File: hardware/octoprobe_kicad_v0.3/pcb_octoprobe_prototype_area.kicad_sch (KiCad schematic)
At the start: 15 parts, among them J1101 Conn_01x20, J1102 Conn_01x20, J1103 Conn_01x20

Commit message: PCB: Octobus
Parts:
- J1101, J1102, J1103: footprint 00_project_library:PinSocket_2x20_P2.54mm_Vertical-mirrored-stackable -> 00_project_library:PinSocket_2x20_P2.54mm_Vertical-stackable_squarepad; symbol Connector_Generic:Conn_02x20_Odd_Even -> Connector_Generic:Conn_01x40; now in the parts list
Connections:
- net at J1101.10 (Pin_10), J1102.10 (Pin_10), J1103.10 (Pin_10): no longer J1101.9 (Pin_9), J1102.9 (Pin_9), J1103.9 (Pin_9)
- net at J1101.11 (Pin_11), J1102.11 (Pin_11), J1103.11 (Pin_11): no longer J1101.12 (Pin_12), J1102.12 (Pin_12), J1103.12 (Pin_12)
- net at J1101.13 (Pin_13), J1102.13 (Pin_13), J1103.13 (Pin_13): no longer J1101.14 (Pin_14), J1102.14 (Pin_14), J1103.14 (Pin_14)
- net at J1101.15 (Pin_15), J1102.15 (Pin_15), J1103.15 (Pin_15): no longer J1101.16 (Pin_16), J1102.16 (Pin_16), J1103.16 (Pin_16)
- net at J1101.17 (Pin_17), J1102.17 (Pin_17), J1103.17 (Pin_17): no longer J1101.18 (Pin_18), J1102.18 (Pin_18), J1103.18 (Pin_18)
- net at J1101.19 (Pin_19), J1102.19 (Pin_19), J1103.19 (Pin_19): no longer J1101.20 (Pin_20), J1102.20 (Pin_20), J1103.20 (Pin_20)
- net at J1101.21 (Pin_21), J1102.21 (Pin_21), J1103.21 (Pin_21): no longer J1101.22 (Pin_22), J1102.22 (Pin_22), J1103.22 (Pin_22)
- net at J1101.23 (Pin_23), J1102.23 (Pin_23), J1103.23 (Pin_23): no longer J1101.24 (Pin_24), J1102.24 (Pin_24), J1103.24 (Pin_24)
- net at J1101.25 (Pin_25), J1102.25 (Pin_25), J1103.25 (Pin_25): no longer J1101.26 (Pin_26), J1102.26 (Pin_26), J1103.26 (Pin_26)
- net at J1101.27 (Pin_27), J1102.27 (Pin_27), J1103.27 (Pin_27): no longer J1101.28 (Pin_28), J1102.28 (Pin_28), J1103.28 (Pin_28)
- net at J1101.29 (Pin_29), J1102.29 (Pin_29), J1103.29 (Pin_29): no longer J1101.30 (Pin_30), J1102.30 (Pin_30), J1103.30 (Pin_30)
- net at J1101.31 (Pin_31), J1102.31 (Pin_31), J1103.31 (Pin_31): no longer J1101.32 (Pin_32), J1102.32 (Pin_32), J1103.32 (Pin_32)
- net at J1101.33 (Pin_33), J1102.33 (Pin_33), J1103.33 (Pin_33): no longer J1101.34 (Pin_34), J1102.34 (Pin_34), J1103.34 (Pin_34)
- net at J1101.35 (Pin_35), J1102.35 (Pin_35), J1103.35 (Pin_35): no longer J1101.36 (Pin_36), J1102.36 (Pin_36), J1103.36 (Pin_36)
- net at J1101.5 (Pin_5), J1102.5 (Pin_5), J1103.5 (Pin_5): no longer J1101.6 (Pin_6), J1102.6 (Pin_6), J1103.6 (Pin_6)
- net at J1101.7 (Pin_7), J1102.7 (Pin_7), J1103.7 (Pin_7): no longer J1101.8 (Pin_8), J1102.8 (Pin_8), J1103.8 (Pin_8)
- new net: J1101.12 (Pin_12), J1102.12 (Pin_12), J1103.12 (Pin_12)
- new net: J1101.14 (Pin_14), J1102.14 (Pin_14), J1103.14 (Pin_14)
- new net: J1101.16 (Pin_16), J1102.16 (Pin_16), J1103.16 (Pin_16)
- new net: J1101.18 (Pin_18), J1102.18 (Pin_18), J1103.18 (Pin_18)
- new net: J1101.20 (Pin_20), J1102.20 (Pin_20), J1103.20 (Pin_20)
- new net: J1101.22 (Pin_22), J1102.22 (Pin_22), J1103.22 (Pin_22)
- new net: J1101.24 (Pin_24), J1102.24 (Pin_24), J1103.24 (Pin_24)
- new net: J1101.26 (Pin_26), J1102.26 (Pin_26), J1103.26 (Pin_26)
- new net: J1101.28 (Pin_28), J1102.28 (Pin_28), J1103.28 (Pin_28)
- new net: J1101.30 (Pin_30), J1102.30 (Pin_30), J1103.30 (Pin_30)
- new net: J1101.32 (Pin_32), J1102.32 (Pin_32), J1103.32 (Pin_32)
- new net: J1101.34 (Pin_34), J1102.34 (Pin_34), J1103.34 (Pin_34)
- new net: J1101.36 (Pin_36), J1102.36 (Pin_36), J1103.36 (Pin_36)
- new net: J1101.6 (Pin_6), J1102.6 (Pin_6), J1103.6 (Pin_6)
- new net: J1101.8 (Pin_8), J1102.8 (Pin_8), J1103.8 (Pin_8)
- new net: J1101.9 (Pin_9), J1102.9 (Pin_9), J1103.9 (Pin_9)
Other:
- moved on the sheet: J1101, J1102, J1103

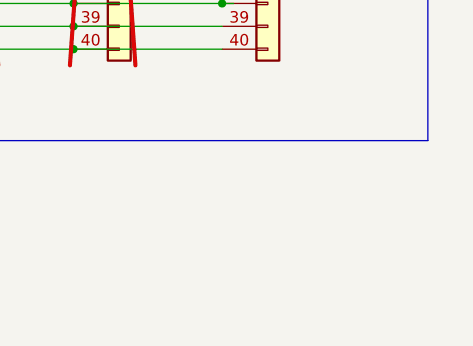
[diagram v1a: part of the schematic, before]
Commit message: PCB: Add "Open Hardware"
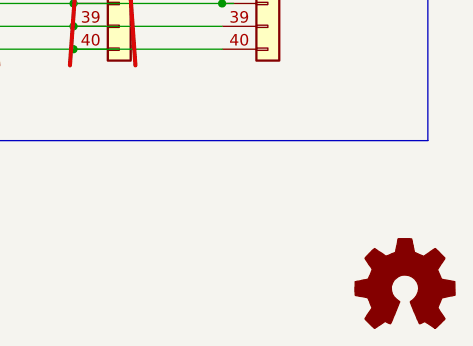
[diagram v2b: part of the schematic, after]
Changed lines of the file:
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@@
+	)
+	(symbol
+		(lib_id "Graphic:Logo_Open_Hardware_Small")
+		(at 275.59 173.99 0)
+		(unit 1)
+		(exclude_from_sim yes)
+		(in_bom no)
+		(on_board no)
+		(dnp no)
+		(fields_autoplaced yes)
+		(property "Reference" "#SYM1301"
+			(at 275.59 167.005 0)
+			(effects
+				(font
+					(size 1.27 1.27)
+				)
+				(hide yes)
+			)
+		)
+		(property "Value" "Logo_Open_Hardware_Small"
+			(at 275.59 179.705 0)
+			(effects
+				(font
+					(size 1.27 1.27)
+				)
+				(hide yes)
+			)
+		)
+		(property "Footprint" ""
+			(at 275.59 173.99 0)
+			(effects
+				(font
+					(size 1.27 1.27)
+				)
+				(hide yes)
+			)
+		)
+		(property "Datasheet" "~"
+			(at 275.59 173.99 0)
+			(effects
+				(font
+					(size 1.27 1.27)
+				)
+				(hide yes)
+			)
+		)
+		(property "Description" "Open Hardware logo, small"
+			(at 275.59 173.99 0)
+			(effects
+				(font
+					(size 1.27 1.27)
+				)
+				(hide yes)
+			)
+		)
+		(instances
+			(project "pcb_octoprobe"
+				(path "/35c47459-45a7-4753-acae-c8b47e7575e1/290edc0f-259a-4a81-bb28-767ae8aa5342"
+					(reference "#SYM1301")
+					(unit 1)
+				)
+			)
+		)
 	)
 	(symbol

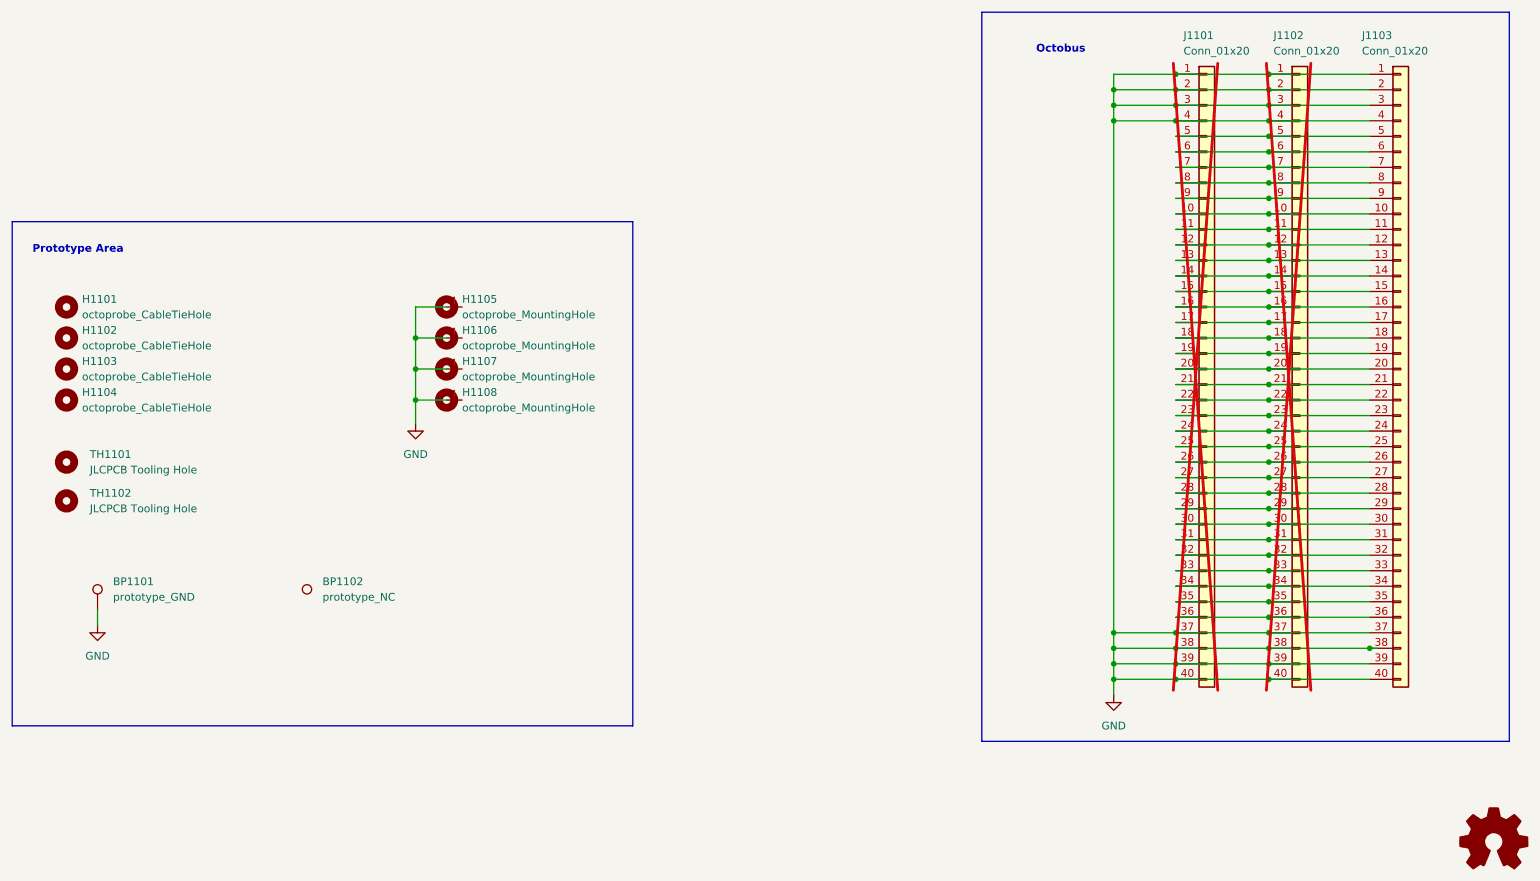
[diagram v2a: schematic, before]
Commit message: PCB: Production files ready
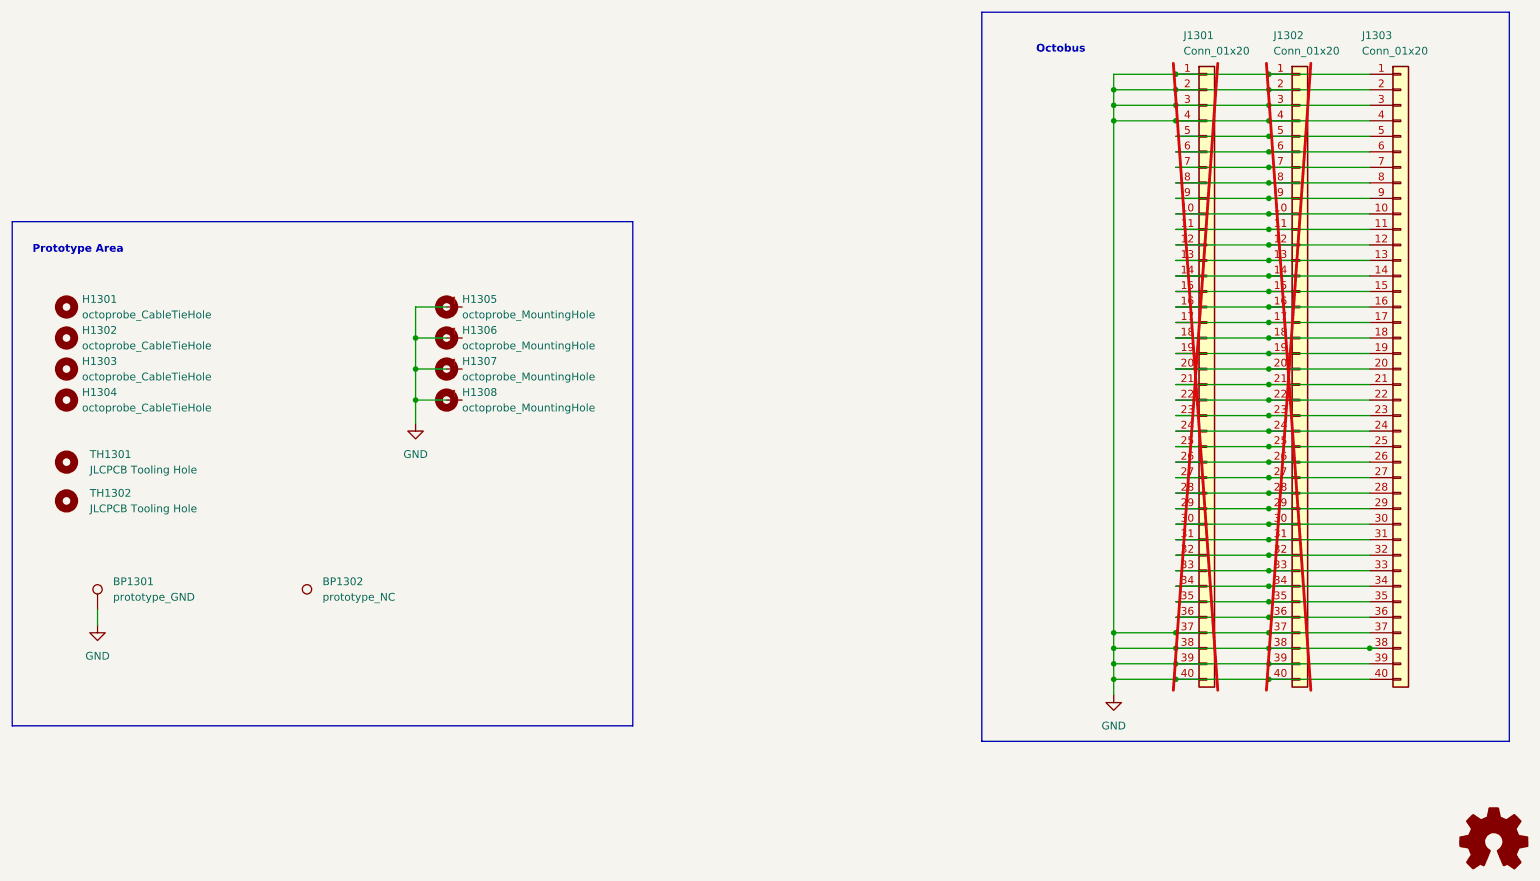
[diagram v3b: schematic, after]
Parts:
- J1301: renamed from J1101; now left out of the parts list
- J1302: renamed from J1102; now left out of the parts list
- J1303: renamed from J1103; now left out of the parts list
- renumbered BP1101 to BP1301, BP1102 to BP1302, H1101 to H1301, H1102 to H1302, H1103 to H1303, H1104 to H1304, H1105 to H1305, H1106 to H1306, H1107 to H1307, H1108 to H1308, TH1101 to TH1301, TH1102 to TH1302
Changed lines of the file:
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@@
 	(title_block
 		(title "Octoprobe tentacle")
-		(date "2024-07-31")
+		(date "2024-08-04")
 		(rev "0.3")
 		(company "Hans Märki, Märki Informatik")
@@
 		(dnp no)
 		(fields_autoplaced yes)
-		(property "Reference" "H1108"
+		(property "Reference" "H1308"
 			(at 106.68 100.3299 0)
 			(effects
@@
 			(project "pcb_octoprobe"
 				(path "/35c47459-45a7-4753-acae-c8b47e7575e1/290edc0f-259a-4a81-bb28-767ae8aa5342"
-					(reference "H1108")
+					(reference "H1308")
 					(unit 1)
 				)
@@
 		(dnp no)
 		(fields_autoplaced yes)
-		(property "Reference" "H1105"
+		(property "Reference" "H1305"
 			(at 106.68 85.0899 0)
 			(effects
@@
 			(project "pcb_octoprobe"
 				(path "/35c47459-45a7-4753-acae-c8b47e7575e1/290edc0f-259a-4a81-bb28-767ae8aa5342"
-					(reference "H1105")
+					(reference "H1305")
 					(unit 1)
 				)
@@
 		(unit 1)
 		(exclude_from_sim no)
-		(in_bom yes)
+		(in_bom no)
 		(on_board yes)
 		(dnp yes)
-		(property "Reference" "J1101"
+		(property "Reference" "J1301"
 			(at 224.79 41.91 0)
 			(effects
@@
 			(project "pcb_octoprobe"
 				(path "/35c47459-45a7-4753-acae-c8b47e7575e1/290edc0f-259a-4a81-bb28-767ae8aa5342"
-					(reference "J1101")
+					(reference "J1301")
 					(unit 1)
 				)
@@
 		(dnp no)
 		(fields_autoplaced yes)
-		(property "Reference" "H1106"
+		(property "Reference" "H1306"
 			(at 106.68 90.1699 0)
 			(effects
@@
 			(project "pcb_octoprobe"
 				(path "/35c47459-45a7-4753-acae-c8b47e7575e1/290edc0f-259a-4a81-bb28-767ae8aa5342"
-					(reference "H1106")
+					(reference "H1306")
 					(unit 1)
 				)
@@
 		(dnp no)
 		(fields_autoplaced yes)
-		(property "Reference" "#PWR01102"
+		(property "Reference" "#PWR01302"
 			(at 99.06 111.76 0)
 			(effects
@@
 			(project "pcb_octoprobe"
 				(path "/35c47459-45a7-4753-acae-c8b47e7575e1/290edc0f-259a-4a81-bb28-767ae8aa5342"
-					(reference "#PWR01102")
+					(reference "#PWR01302")
 					(unit 1)
 				)
@@
 		(dnp no)
 		(fields_autoplaced yes)
-		(property "Reference" "H1103"
+		(property "Reference" "H1303"
 			(at 44.45 95.2499 0)
 			(effects
@@
 			(project "pcb_octoprobe"
 				(path "/35c47459-45a7-4753-acae-c8b47e7575e1/290edc0f-259a-4a81-bb28-767ae8aa5342"
-					(reference "H1103")
+					(reference "H1303")
 					(unit 1)
 				)
@@
 		(dnp no)
 		(fields_autoplaced yes)
-		(property "Reference" "H1107"
+		(property "Reference" "H1307"
 			(at 106.68 95.2499 0)
 			(effects
@@
 			(project "pcb_octoprobe"
 				(path "/35c47459-45a7-4753-acae-c8b47e7575e1/290edc0f-259a-4a81-bb28-767ae8aa5342"
-					(reference "H1107")
+					(reference "H1307")
 					(unit 1)
 				)
@@
 		(dnp no)
 		(fields_autoplaced yes)
-		(property "Reference" "#PWR01101"
+		(property "Reference" "#PWR01301"
 			(at 46.99 144.78 0)
 			(effects
@@
 			(project "pcb_octoprobe"
 				(path "/35c47459-45a7-4753-acae-c8b47e7575e1/290edc0f-259a-4a81-bb28-767ae8aa5342"
-					(reference "#PWR01101")
+					(reference "#PWR01301")
 					(unit 1)
 				)
@@
 		(on_board yes)
 		(dnp no)
-		(property "Reference" "TH1102"
+		(property "Reference" "TH1302"
 			(at 45.72 116.84 0)
 			(effects
@@
 			(project "pcb_octoprobe"
 				(path "/35c47459-45a7-4753-acae-c8b47e7575e1/290edc0f-259a-4a81-bb28-767ae8aa5342"
-					(reference "TH1102")
+					(reference "TH1302")
 					(unit 1)
 				)
@@
 		(on_board yes)
 		(dnp no)
-		(property "Reference" "TH1101"
+		(property "Reference" "TH1301"
 			(at 45.72 110.49 0)
 			(effects
@@
 			(project ""
 				(path "/35c47459-45a7-4753-acae-c8b47e7575e1/290edc0f-259a-4a81-bb28-767ae8aa5342"
-					(reference "TH1101")
+					(reference "TH1301")
 					(unit 1)
 				)
@@
 		(dnp no)
 		(fields_autoplaced yes)
-		(property "Reference" "H1101"
+		(property "Reference" "H1301"
 			(at 44.45 85.0899 0)
 			(effects
@@
 			(project "pcb_octoprobe"
 				(path "/35c47459-45a7-4753-acae-c8b47e7575e1/290edc0f-259a-4a81-bb28-767ae8aa5342"
-					(reference "H1101")
+					(reference "H1301")
 					(unit 1)
 				)
@@
 		(dnp no)
 		(fields_autoplaced yes)
-		(property "Reference" "#PWR01103"
+		(property "Reference" "#PWR01303"
 			(at 213.36 156.21 0)
 			(effects
@@
 			(project "pcb_octoprobe"
 				(path "/35c47459-45a7-4753-acae-c8b47e7575e1/290edc0f-259a-4a81-bb28-767ae8aa5342"
-					(reference "#PWR01103")
+					(reference "#PWR01303")
 					(unit 1)
 				)
@@
 		(dnp no)
 		(fields_autoplaced yes)
-		(property "Reference" "H1102"
+		(property "Reference" "H1302"
 			(at 44.45 90.1699 0)
 			(effects
@@
 			(project "pcb_octoprobe"
 				(path "/35c47459-45a7-4753-acae-c8b47e7575e1/290edc0f-259a-4a81-bb28-767ae8aa5342"
-					(reference "H1102")
+					(reference "H1302")
 					(unit 1)
 				)
@@
 		(dnp no)
 		(fields_autoplaced yes)
-		(property "Reference" "BP1101"
+		(property "Reference" "BP1301"
 			(at 49.53 131.3179 0)
 			(effects
@@
 			(project "pcb_octoprobe"
 				(path "/35c47459-45a7-4753-acae-c8b47e7575e1/290edc0f-259a-4a81-bb28-767ae8aa5342"
-					(reference "BP1101")
+					(reference "BP1301")
 					(unit 1)
 				)
@@
 		(unit 1)
 		(exclude_from_sim no)
-		(in_bom yes)
+		(in_bom no)
 		(on_board yes)
 		(dnp no)
-		(property "Reference" "J1103"
+		(property "Reference" "J1303"
 			(at 254 41.91 0)
 			(effects
@@
 			(project "pcb_octoprobe"
 				(path "/35c47459-45a7-4753-acae-c8b47e7575e1/290edc0f-259a-4a81-bb28-767ae8aa5342"
-					(reference "J1103")
+					(reference "J1303")
 					(unit 1)
 				)
@@
 		(dnp no)
 		(fields_autoplaced yes)
-		(property "Reference" "H1104"
+		(property "Reference" "H1304"
 			(at 44.45 100.3299 0)
 			(effects
@@
 			(project "pcb_octoprobe"
 				(path "/35c47459-45a7-4753-acae-c8b47e7575e1/290edc0f-259a-4a81-bb28-767ae8aa5342"
-					(reference "H1104")
+					(reference "H1304")
 					(unit 1)
 				)
@@
 		(unit 1)
 		(exclude_from_sim no)
-		(in_bom yes)
+		(in_bom no)
 		(on_board yes)
 		(dnp yes)
-		(property "Reference" "J1102"
+		(property "Reference" "J1302"
 			(at 239.522 41.91 0)
 			(effects
@@
 			(project "pcb_octoprobe"
 				(path "/35c47459-45a7-4753-acae-c8b47e7575e1/290edc0f-259a-4a81-bb28-767ae8aa5342"
-					(reference "J1102")
+					(reference "J1302")
 					(unit 1)
 				)
@@
 		(dnp no)
 		(fields_autoplaced yes)
-		(property "Reference" "BP1102"
+		(property "Reference" "BP1302"
 			(at 83.82 131.3179 0)
 			(effects
@@
 			(project "pcb_octoprobe"
 				(path "/35c47459-45a7-4753-acae-c8b47e7575e1/290edc0f-259a-4a81-bb28-767ae8aa5342"
-					(reference "BP1102")
+					(reference "BP1302")
 					(unit 1)
 				)
